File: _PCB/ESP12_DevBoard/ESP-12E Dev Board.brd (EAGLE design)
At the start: 52 x 60 mm, 48 parts, among them J1 ZX62-B-5PA(33), J10 DUST, J11 BTN2, J2 I2C, J3 LCD, J4 I2C, J5 LCD_BACKLIGHT, J6 TEMP/HUM, J7 RADON, J8 BTN1, J9 ADC, Q1 UMH3N, U1 5V_REG, U2 3V3_REG, U3 CH340C, U4 TXB0104

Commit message: final edit sample edit
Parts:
- moved J5 12.4 mm to (1.78, 8.17), turned to 90 degrees
- moved JP1 3.14 mm to (11.7, 6.64), turned to 180 degrees
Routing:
- net LED+: track 36.7 -> 27.2 mm
- net GND: track 53.6 -> 61.7 mm, vias 40 -> 42
- net N$3: track 8.94 -> 15.4 mm
- net 5V: track 191.2 -> 189.9 mm, vias 3 -> 4
- net POWER: track 55.3 -> 54.1 mm
- net POWER1: track 31.3 -> 30.3 mm

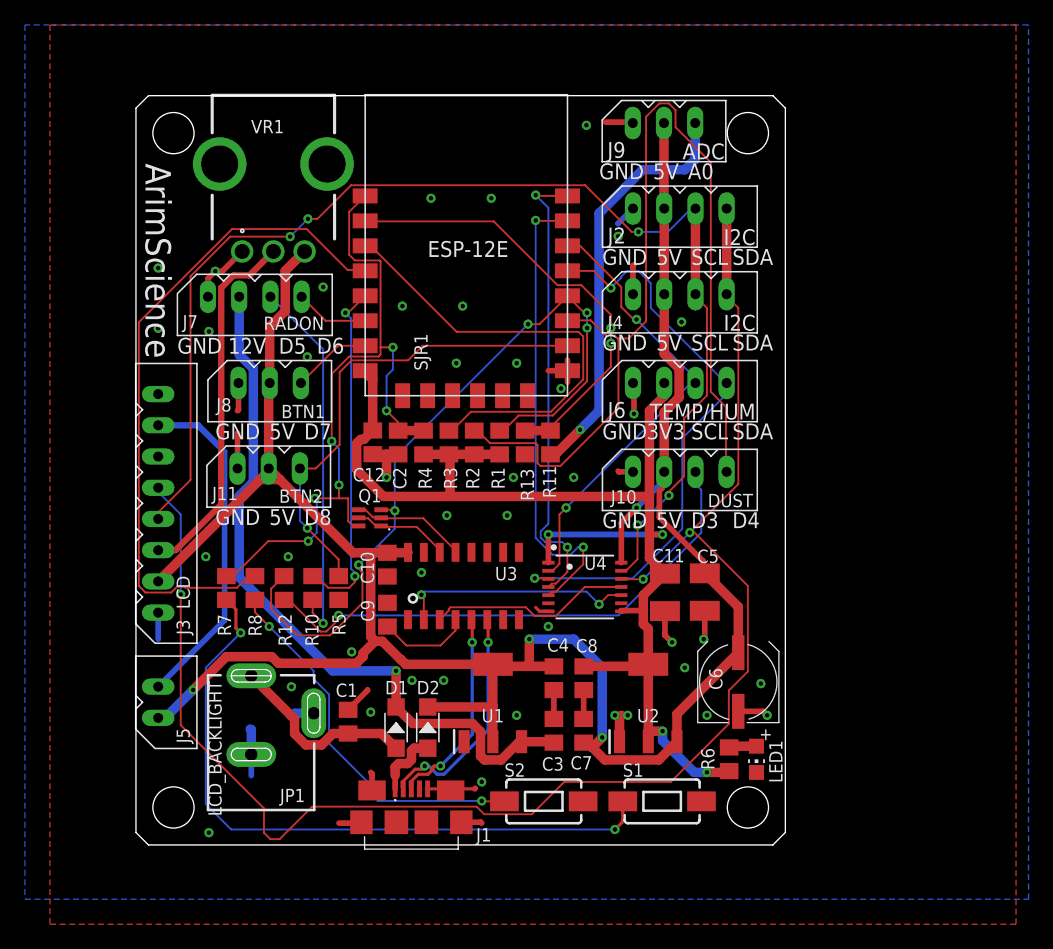
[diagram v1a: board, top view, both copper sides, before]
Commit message: V1.2: GND plane issue fixed + optimized routes
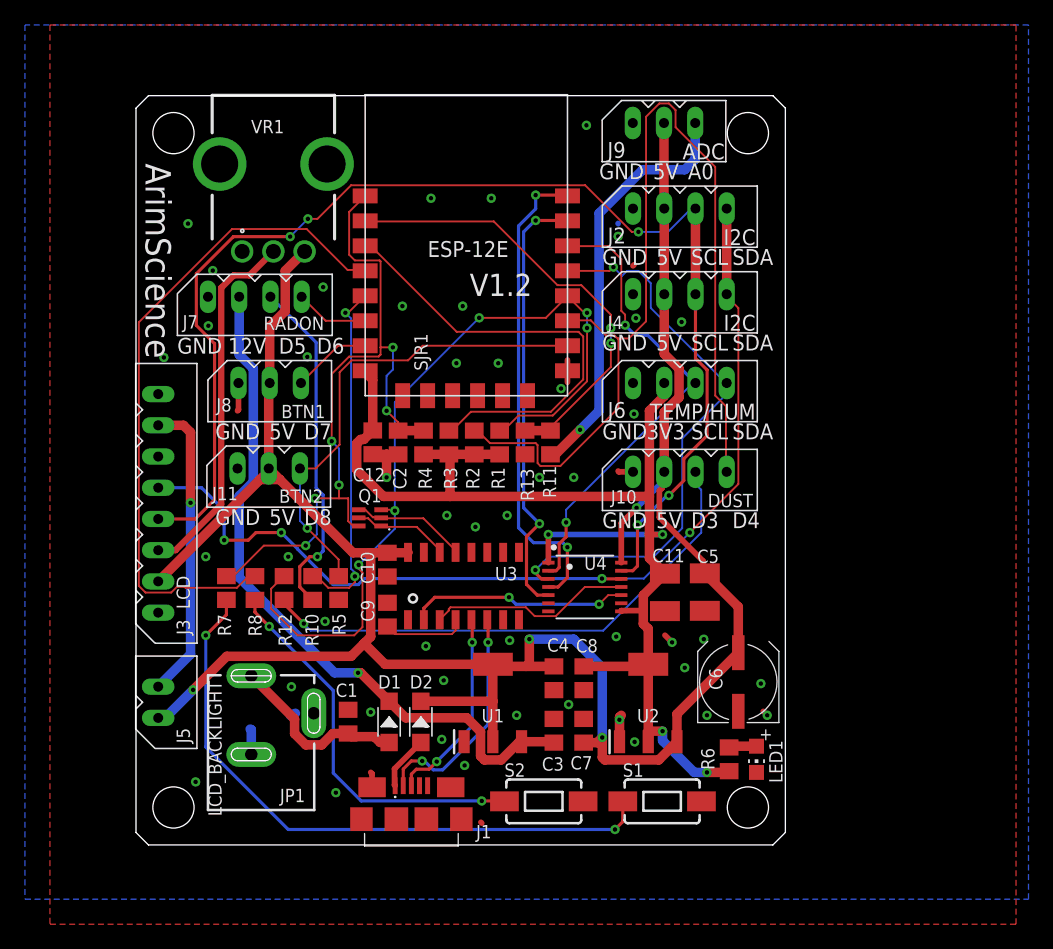
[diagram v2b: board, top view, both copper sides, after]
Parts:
- moved D1 0.72 mm to (20.3, 7.86)
- moved D2 0.72 mm to (22.8, 7.86)
- moved J1 0.25 mm to (22.1, 0.79)
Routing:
- net SDA_5V: track 126.1 -> 78.9 mm, vias 3 -> 4
- net GND: track 61.7 -> 16.8 mm, vias 42 -> 47
- net GPIO0: track 61.9 -> 65.6 mm
- net POWER: track 54.1 -> 50.5 mm
- net SCL_5V: track 98.8 -> 101.9 mm
- net LED+: track 27.2 -> 24.3 mm, vias 0 -> 1
- net RXD: track 37.8 -> 35.2 mm
- net N$6: track 30.1 -> 27.6 mm
- net 12V: track 58.1 -> 56.4 mm
- net GPIO5: track 36.5 -> 38.1 mm
- net TXD: track 37.1 -> 38.6 mm
- net RXD_5V: track 18.9 -> 17.6 mm
- net 5V_INPUT: track 5.41 -> 4.35 mm
- net POWER1: track 30.3 -> 31.1 mm
- net N$1: track 7.45 -> 6.69 mm
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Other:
- board text added: "V1.2"

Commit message: PCB V1.3 update
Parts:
- removed R7: 470Ω, rcl:R0805
- added C13: 220uF, rcl:UD-6,3X7,7_NICHICON
- added C14: 100nF, rcl:C0805
- added R14, R9: 10k, rcl:R0805
- C6: value 220uF(optional) -> 220uF
- R6: value 470Ω -> 10k
- moved C11 27.7 mm to (17.4, 30.3)
- moved C5 4.93 mm to (48.7, 22.0), turned to 0 degrees
- moved C1 2.17 mm to (19.1, 8.43), turned to 90 degrees
- moved D1 1.37 mm to (21.0, 9.02)
- moved D2 1.23 mm to (23.0, 9.07)
- moved R11 1.12 mm to (34.3, 30.3)
- moved R13 1.12 mm to (32.3, 30.3)
- moved R1 1.12 mm to (30.2, 30.3)
- moved R2 1.12 mm to (28.2, 30.3)
- moved R3 1.12 mm to (26.2, 30.3)
- moved R4 1.12 mm to (24.1, 30.3)
- moved C12 1.10 mm to (20.1, 30.3), turned to 270 degrees
- moved C2 1.10 mm to (22.1, 30.3), turned to 270 degrees
- moved R10 1.02 mm to (13.1, 18.6)
- moved R12 1.02 mm to (10.8, 18.6)
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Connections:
- removed net 5V_INPUT: D2.+, J1.VCC
- removed net POWER: R7.2, S1.1
- new net N$10: C14.2, D2.+, J1.VCC
- new net N$7: R9.2, U3.13
- new net N$8: R14.2, U3.14
- net 3.3V: now also C13.+
- net DTR: now also R9.1; no longer U3.13
- net GND: now also C13.-, C14.1
- net GPIO0: now also R8.1
- net GPIO16: no longer R8.1
- net RST: now also S1.1; no longer R7.1
- net RTS: now also R14.1; no longer U3.14
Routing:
- net RST: track 57.6 -> 116.5 mm
- net GPIO16: track 53.8 -> 0.00 mm
- net POWER: track 50.5 -> 0.00 mm, vias 2 -> 0
- net 5V: track 189.7 -> 169.3 mm, vias 4 -> 5
- net EN: track 36.4 -> 20.4 mm, vias 0 -> 2
- net N$10: track 0.00 -> 11.5 mm
- net GPIO4: track 45.9 -> 53.2 mm
- net GND: track 16.8 -> 9.57 mm, vias 47 -> 51
- net ADC: track 36.1 -> 29.0 mm, vias 2 -> 1
- net N$7: track 0.00 -> 4.85 mm
- net 5V_INPUT: track 4.35 -> 0.00 mm
- net 12V: track 56.4 -> 60.4 mm
- net DTR: track 9.26 -> 6.51 mm
- net N$8: track 0.00 -> 2.61 mm
- net GPIO14: track 28.0 -> 30.4 mm
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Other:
- board text added: "V1.3"
- board text removed: "V1.2"

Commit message: optimization _ gerber errors
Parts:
- removed C7: 10uF, rcl:C0805
- moved C3 1.35 mm to (34.5, 6.11), turned to 0 degrees
- moved C2 0.41 mm to (22.1, 29.9)
- moved C12 0.41 mm to (20.1, 29.9)
- moved R1 0.36 mm to (30.2, 29.9)
- moved R2 0.36 mm to (28.2, 29.9)
- moved R3 0.36 mm to (26.2, 29.9)
- moved R4 0.36 mm to (24.1, 29.9)
- moved R11 0.36 mm to (34.3, 29.9)
- moved R13 0.36 mm to (32.3, 29.9)
- moved C11 0.31 mm to (17.4, 30.0)
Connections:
- net 5V: no longer C7.1
- net GND: no longer C7.2
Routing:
- net 5V: track 169.3 -> 177.6 mm, vias 5 -> 2
- net ADC: track 29.0 -> 26.8 mm, vias 1 -> 0
- net GPIO0: track 67.0 -> 65.2 mm
- net 3.3V: track 99.4 -> 100.2 mm
- net 12V: track 60.4 -> 59.7 mm
- net GND: track 9.57 -> 9.23 mm, vias 51 -> 55

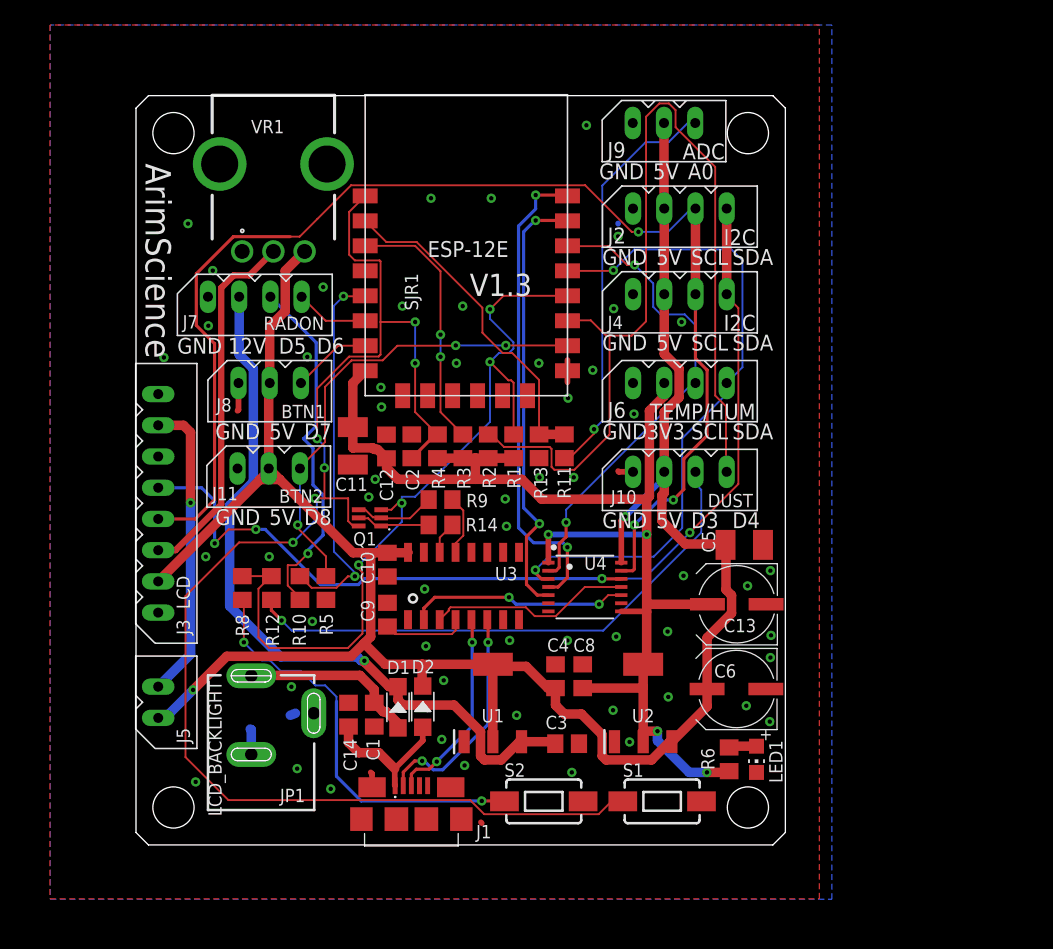
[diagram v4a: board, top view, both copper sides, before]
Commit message: PCB edit, broken gerber, BOM to be updated
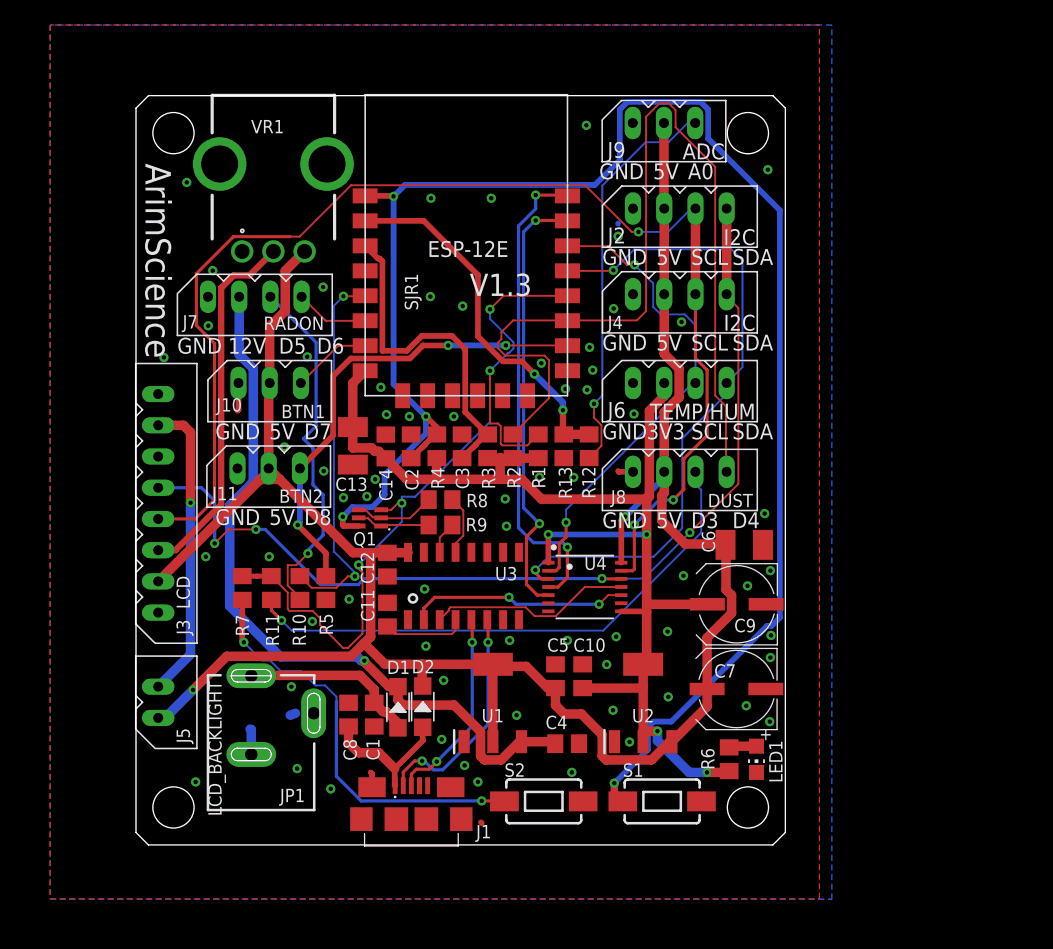
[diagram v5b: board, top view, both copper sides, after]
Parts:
- removed R14: 10k, rcl:R0805
- added C7: 220uF, rcl:UD-6,3X7,7_NICHICON
- added R7: 470Ω, rcl:R0805
- C10: value 100nF -> 22uF
- C11: value 100uF -> 100nF; device rcl:SMC_B -> rcl:C0805
- C13, C6: value 220uF -> 100uF; device rcl:UD-6,3X7,7_NICHICON -> rcl:SMC_B
- C3: value 10uF -> 100nF
- C4: value 22uF -> 10uF
- C5: value 100uF -> 22uF; device rcl:SMC_B -> rcl:C0805
- C8: value 22uF -> 100nF
- C9: value 100nF -> 220uF; device rcl:C0805 -> rcl:UD-6,3X7,7_NICHICON
- J10: value DUST -> BTN1; device con-molex-spox:5267-4 -> con-molex-spox:5267-3
- J8: value BTN1 -> DUST; device con-molex-spox:5267-3 -> con-molex-spox:5267-4
- R11: value 47k(1%) -> 470Ω
- R12: value 470Ω -> 47k(1%)
- R8: value 470Ω -> 4.7k
- R9: value 10k -> 4.7k
- moved C13 33.3 mm to (17.4, 30.0), turned to 270 degrees
- moved J10 32.4 mm to (8.21, 35.0)
- moved J8 32.4 mm to (39.8, 27.9)
- moved C9 28.0 mm to (48.1, 17.3), turned to 180 degrees
- moved R12 27.9 mm to (36.3, 29.9)
- moved R11 26.1 mm to (10.8, 18.6)
- moved C3 25.3 mm to (26.1, 29.9), turned to 270 degrees
- moved C14 21.7 mm to (20.0, 29.9)
- moved C8 19.0 mm to (17.0, 8.43)
- moved C5 18.4 mm to (33.6, 11.5), turned to 90 degrees
- moved C10 18.0 mm to (35.8, 11.5), turned to 270 degrees
- moved R8 17.4 mm to (24.4, 25.7), turned to 0 degrees
- moved C11 13.8 mm to (20.1, 16.4)
- moved C6 11.6 mm to (48.7, 22.0), turned to 0 degrees
- moved C12 9.46 mm to (20.1, 20.4), turned to 90 degrees
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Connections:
- net 12V: now also C4.1; no longer C3.1
- net 3.3V: now also C10.2, C14.2, C9.+; no longer C11.+, C12.2, C8.2
- net 5V: now also C12.2, C5.1, C7.+; no longer C10.2, C4.1, C5.+
- net ADC: now also R12.1; no longer R11.1
- net DTR: now also R8.1; no longer R9.1
- net EN: now also C3.2
- net GND: now also C11.1, C3.1, C5.2, C7.-, C9.-; no longer C11.-, C3.2, C5.-, C9.1
- net GPIO0: now also R11.1, R7.1; no longer R12.1, R8.1
- net GPIO13: now also J10.P$3; no longer J8.P$3
- net GPIO2: now also J8.P$4; no longer J10.P$4
- net N$1: now also C11.2; no longer C9.2
- net N$10: now also C8.2; no longer C14.2
- net N$5: now also R12.2; no longer R11.2
- net N$7: now also R8.2; no longer R9.2
- net N$8: now also R9.2; no longer R14.2
- net N$9: now also J8.P$3, R11.2; no longer J10.P$3, R12.2
- net POWER1: now also R7.2; no longer R8.2
- net RTS: now also R9.1; no longer R14.1
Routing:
- net RST: track 116.5 -> 136.3 mm, vias 6 -> 4
- net EN: track 20.7 -> 27.1 mm, vias 2 -> 0
- net GPIO2: track 78.2 -> 74.9 mm
- net ADC: track 26.8 -> 29.3 mm, vias 0 -> 2
- net GND: track 9.23 -> 7.45 mm, vias 55 -> 66
